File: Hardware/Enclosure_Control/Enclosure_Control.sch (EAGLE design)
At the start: 22 parts, among them M1 ARDUINO-NANO-3.0, Q1 IRF3704, Q2 IRF3704, Q3 IRF3704, Q4 IRF3704

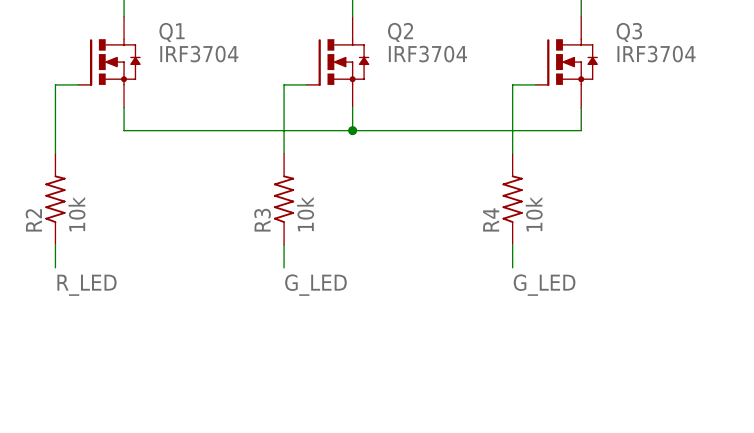
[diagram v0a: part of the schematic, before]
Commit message: Añadimos Extruder_Hotend cable
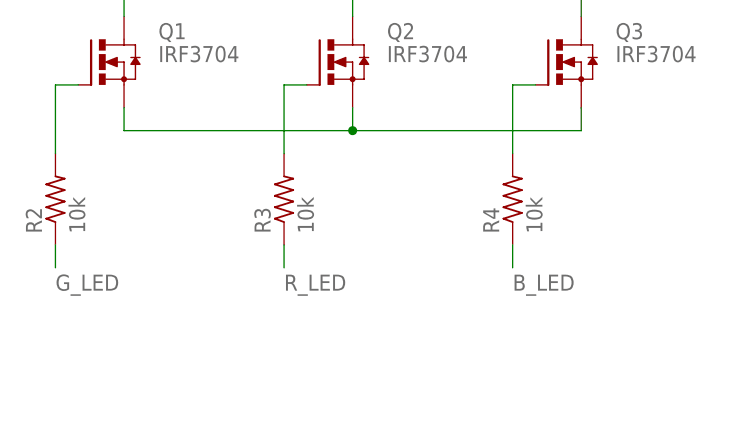
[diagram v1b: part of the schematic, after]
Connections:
- net B_LED: now also R4.1
- net G_LED: now also R2.1; no longer R3.1, R4.1
- net R_LED: now also R3.1; no longer R2.1
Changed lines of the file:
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@@
 <setting verticaltext="up"/>
 </settings>
-<grid distance="0.1" unitdist="inch" unit="inch" style="dots" multiple="1" display="yes" altdistance="0.01" altunitdist="inch" altunit="inch"/>
+<grid distance="0.1" unitdist="inch" unit="inch" style="lines" multiple="1" display="no" altdistance="0.01" altunitdist="inch" altunit="inch"/>
 <layers>
 <layer number="1" name="Top" color="4" fill="1" visible="no" active="no"/>
@@
 <label x="53.34" y="127" size="1.778" layer="95"/>
 </segment>
+<segment>
+<pinref part="R4" gate="G$1" pin="1"/>
+<wire x1="63.5" y1="33.02" x2="63.5" y2="30.48" width="0.1524" layer="91"/>
+<label x="63.5" y="27.94" size="1.778" layer="95"/>
+</segment>
 </net>
 <net name="DOOR_S" class="0">
@@
 </segment>
 <segment>
+<pinref part="R2" gate="G$1" pin="1"/>
+<wire x1="12.7" y1="33.02" x2="12.7" y2="30.48" width="0.1524" layer="91"/>
+<label x="12.7" y="27.94" size="1.778" layer="95"/>
+</segment>
+</net>
+<net name="R_LED" class="0">
+<segment>
+<pinref part="M1" gate="G$1" pin="D6"/>
+<wire x1="71.12" y1="119.38" x2="53.34" y2="119.38" width="0.1524" layer="91"/>
+<label x="53.34" y="119.38" size="1.778" layer="95"/>
+</segment>
+<segment>
 <pinref part="R3" gate="G$1" pin="1"/>
 <wire x1="38.1" y1="33.02" x2="38.1" y2="30.48" width="0.1524" layer="91"/>
 <label x="38.1" y="27.94" size="1.778" layer="95"/>
 </segment>
-<segment>
-<pinref part="R4" gate="G$1" pin="1"/>
-<wire x1="63.5" y1="33.02" x2="63.5" y2="30.48" width="0.1524" layer="91"/>
-<label x="63.5" y="27.94" size="1.778" layer="95"/>
-</segment>
 </net>
-<net name="R_LED" class="0">
-<segment>
-<pinref part="M1" gate="G$1" pin="D6"/>
-<wire x1="71.12" y1="119.38" x2="53.34" y2="119.38" width="0.1524" layer="91"/>
-<label x="53.34" y="119.38" size="1.778" layer="95"/>
-</segment>
-<segment>
-<pinref part="R2" gate="G$1" pin="1"/>
-<wire x1="12.7" y1="33.02" x2="12.7" y2="30.48" width="0.1524" layer="91"/>
-<label x="12.7" y="27.94" size="1.778" layer="95"/>
-</segment>
-</net>
